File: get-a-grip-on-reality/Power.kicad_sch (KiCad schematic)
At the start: 3 parts, among them J1 Battery Connector, U1 BQ25170DSGR, U2 TLV76733DRVx

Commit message: power wip
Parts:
- added C1, C2, C3, C4: 1u, symbol Device:C
- added R1: 10K, symbol Device:R
- added R2: 30K-375, symbol Device:R
- added R3: R, symbol Device:R
- added TH1: Thermistor_NTC, symbol Device:Thermistor_NTC
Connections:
- net +BATT: now also U2.4 (EN), U2.6 (IN), C1.1
- net GND: now also U1.4 (GND), U1.8 (OUT), U2.3 (GND), U2.5 (GND), U2.7 (PAD), C1.2, C2.2, C3.2, C4.2, R2.2, R3.2, TH1.2
- net +3.3V: now reaches U2.1 (OUT)
- net +3.3V: now also U2.2 (SNS), C2.1, C3.1
- net +5V: now reaches U1.1 (IN)
- net +5V: now also C4.1
- net at U1.2 (ISET): now also R2.1
- net at U1.3 (TS): now also TH1.1
- net at U1.5 (STAT): now also R1.2
- net at U1.7 (VSET): now also R3.1
- new net VCC: R1.1
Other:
- moved on the sheet: J1, U1, U2

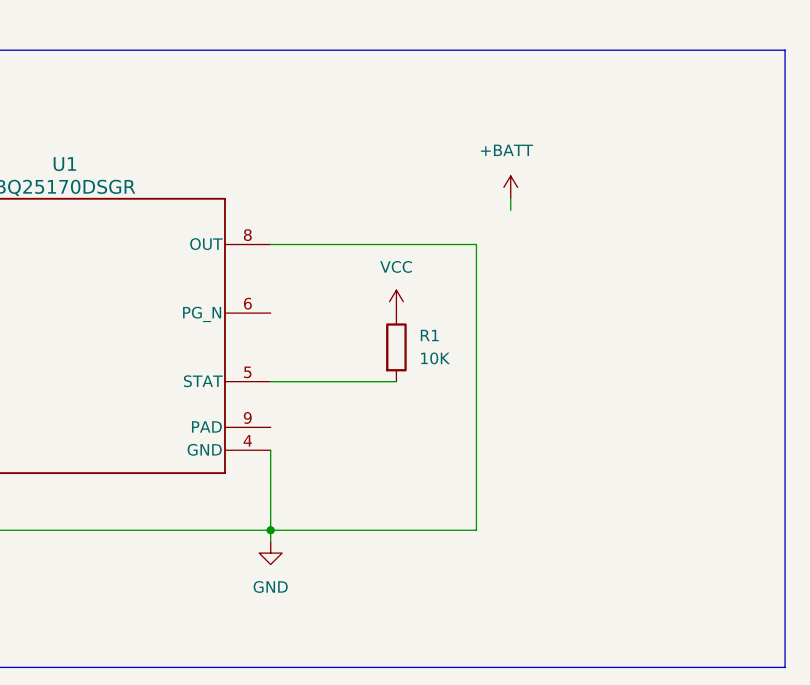
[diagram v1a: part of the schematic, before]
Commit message: power out
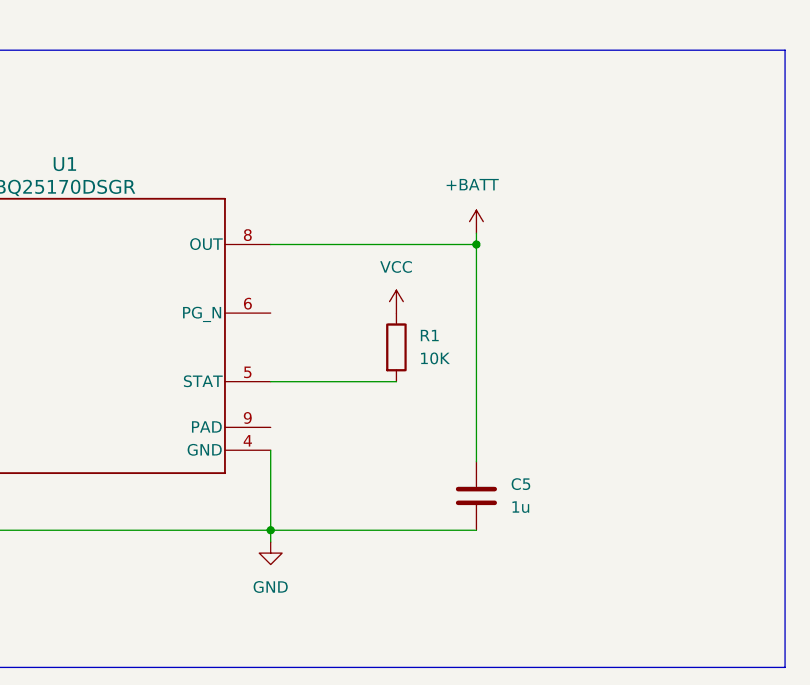
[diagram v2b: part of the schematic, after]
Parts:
- added C5: 1u, symbol Device:C
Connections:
- net +BATT: now also U1.8 (OUT), C5.1
- net GND: now also C5.2; no longer U1.8 (OUT)
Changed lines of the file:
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@@
+	)
+	(junction
+		(at 128.27 78.74)
+		(diameter 0)
+		(color 0 0 0 0)
 	)
 	(junction
@@
 	(wire
 		(pts
+			(xy 128.27 102.87) (xy 128.27 78.74)
+		)
+		(stroke
+			(width 0)
+			(type default)
+		)
+	)
+	(wire
+		(pts
 			(xy 196.85 92.71) (xy 196.85 95.25)
 		)
@@
 	(wire
 		(pts
+			(xy 105.41 110.49) (xy 128.27 110.49)
+		)
+		(stroke
+			(width 0)
+			(type default)
+		)
+	)
+	(wire
+		(pts
 			(xy 231.14 86.36) (xy 231.14 85.09)
 		)
@@
 	(wire
 		(pts
-			(xy 132.08 73.66) (xy 132.08 74.93)
+			(xy 128.27 77.47) (xy 128.27 78.74)
 		)
 		(stroke
@@
 	(wire
 		(pts
-			(xy 128.27 78.74) (xy 128.27 110.49)
-		)
-		(stroke
-			(width 0)
-			(type default)
-		)
-	)
-	(wire
-		(pts
 			(xy 54.61 110.49) (xy 59.69 110.49)
 		)
@@
 		(pts
 			(xy 271.78 91.44) (xy 266.7 91.44)
-		)
-		(stroke
-			(width 0)
-			(type default)
-		)
-	)
-	(wire
-		(pts
-			(xy 128.27 110.49) (xy 105.41 110.49)
 		)
 		(stroke
@@
 	(symbol
 		(lib_id "Device:C")
+		(at 128.27 106.68 0)
+		(unit 1)
+		(exclude_from_sim no)
+		(in_bom yes)
+		(on_board yes)
+		(dnp no)
+		(fields_autoplaced yes)
+		(property "Reference" "C5"
+			(at 132.08 105.4099 0)
+			(effects
+				(font
+					(size 1.27 1.27)
+				)
+				(justify left)
+			)
+		)
+		(property "Value" "1u"
+			(at 132.08 107.9499 0)
+			(effects
+				(font
+					(size 1.27 1.27)
+				)
+				(justify left)
+			)
+		)
+		(property "Footprint" ""
+			(at 129.2352 110.49 0)
+			(effects
+				(font
+					(size 1.27 1.27)
+				)
+				(hide yes)
+			)
+		)
+		(property "Datasheet" "~"
+			(at 128.27 106.68 0)
+			(effects
+				(font
+					(size 1.27 1.27)
+				)
+				(hide yes)
+			)
+		)
+		(property "Description" "Unpolarized capacitor"
+			(at 128.27 106.68 0)
+			(effects
+				(font
+					(size 1.27 1.27)
+				)
+				(hide yes)
+			)
+		)
+		(pin "1"
+		)
+		(pin "2"
+		)
+		(instances
+			(project "get-a-grip-on-reality"
+				(path "/baa0c64e-005f-4609-8fc2-3159870af962/9688e5e2-596f-4b3e-8875-d3add90a032c"
+					(reference "C5")
+					(unit 1)
+				)
+			)
+		)
+	)
+	(symbol
+		(lib_id "Device:C")
 		(at 231.14 90.17 0)
 		(unit 1)
@@
 		(lib_name "+BATT_2")
 		(lib_id "power:+BATT")
-		(at 132.08 73.66 0)
+		(at 128.27 77.47 0)
 		(unit 1)
 		(exclude_from_sim no)
@@
 		(dnp no)
 		(property "Reference" "#PWR09"
-			(at 132.08 77.47 0)
+			(at 128.27 81.28 0)
 			(effects
 				(font
@@
 		)
 		(property "Value" "+BATT"
-			(at 131.572 68.326 0)
+			(at 127.762 72.136 0)
 			(effects
 				(font
@@
 		)
 		(property "Footprint" ""
-			(at 132.08 73.66 0)
+			(at 128.27 77.47 0)
 			(effects
 				(font
@@
 		)
 		(property "Datasheet" ""
-			(at 132.08 73.66 0)
+			(at 128.27 77.47 0)
 			(effects
 				(font
@@
 		)
 		(property "Description" "Power symbol creates a global label with name \"+BATT\""
-			(at 132.08 73.66 0)
-			(effects
-				(font
+			(at 128.27 77.47 0)
+			(effects
+				(font

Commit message: power
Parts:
- removed C4, C5: 1u, symbol Device:C
- removed R1: 10K, symbol Device:R
- removed R3: R, symbol Device:R
- removed U1: BQ25170DSGR, footprints:DSG0008A, symbol bq25170:BQ25170DSGR
- added C10, C13: 2.2u, symbol Device:C
- added C11: 10u, symbol Device:C
- added C12: 0.047u, symbol Device:C
- added D3: LED, symbol Device:LED
- added R10, R11, R8, R9: R, symbol Device:R
- added U1: BQ25306RTER, BQ25306RTER:IC_BQ25306RTER, symbol BQ25306RTER:BQ25306RTER
- R2: value 30K-375 -> <200k
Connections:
- net +5V: now also C10.1, U1.1 (VBUS)
- net +BATT: now also R11.1, U1.10 (BAT)
- net GND: now also TH1.1, C10.2, C11.2, C13.2, R8.1, R9.1, U1.7 (TS); no longer R2.2, TH1.2
- new net: D3.1 (K), U1.3 (STAT)
- new net: C12.1, U1.13 (SW)
- new net: C12.2, U1.15 (BTST)
- new net: C11.1, U1.16 (PMID)
- new net: C13.1, R10.1, R8.2, U1.2 (REGN)
- new net: R9.2, U1.6 (~{EN})
- new net: R2.2, U1.8 (FB_GND)
- new net: R11.2, U1.9 (FB)
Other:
- moved on the sheet: TH1
